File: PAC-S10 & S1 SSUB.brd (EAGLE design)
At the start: 160 x 100 mm, 177 parts, among them IC1 TLV1117, IC10 LM324D, IC14 TC51832F-10, IC15 315-5476A, IC21 TC51832F-10, IC33 LC7881M, IC34 NJM844GD, IC35 MC33079D, IC37 LM4558D, IC38 LM4558D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

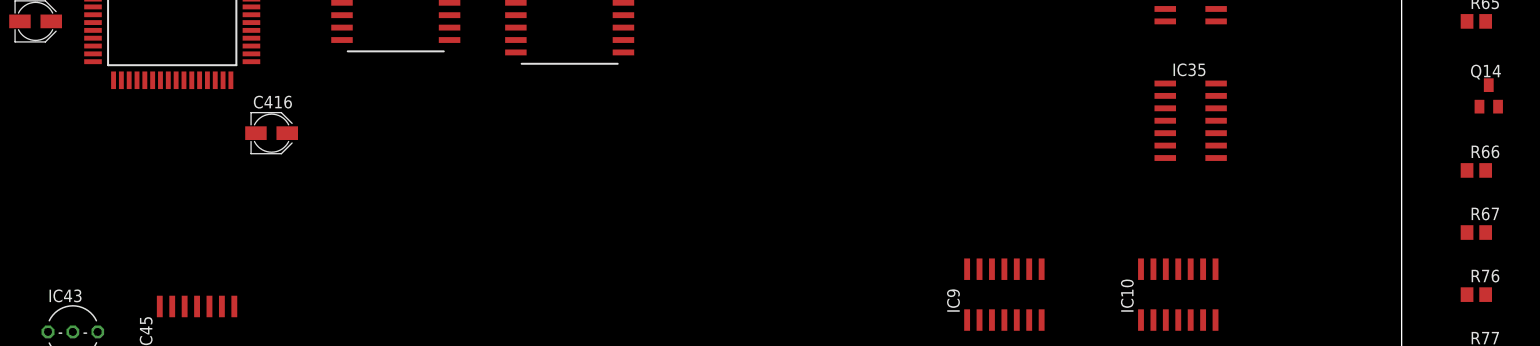
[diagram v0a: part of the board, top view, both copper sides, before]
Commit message: Add files via upload
Q14 is diode connected, uploading corrected files
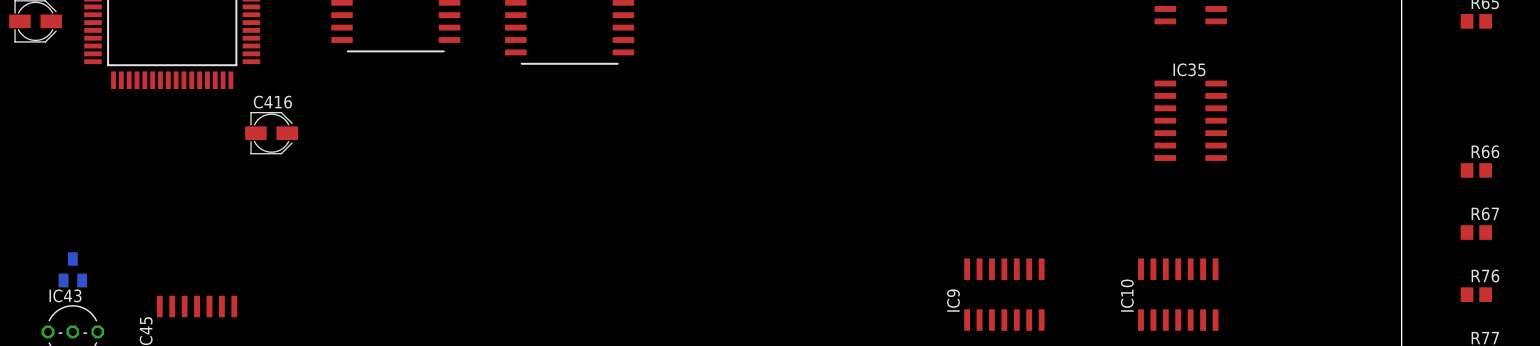
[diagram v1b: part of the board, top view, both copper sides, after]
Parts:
- moved Q14 145.9 mm to (24.1, 17.8), flipped to the bottom
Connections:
- removed net N$23: IC43.3, Q14.C, R65.2, R66.1
- net MRES: now also IC43.3, Q14.C, R65.2, R66.1
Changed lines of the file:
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@@
 <attribute name="VALUE" x="167.005" y="40.64" size="1.27" layer="27"/>
 </element>
-<element name="Q14" library="transistor-pnp" library_urn="urn:adsk.eagle:library:399" package="SOT23-BEC" package3d_urn="urn:adsk.eagle:package:28748/2" value="MMBT3906LT1SMD" x="168.91" y="35.56" smashed="yes">
-<attribute name="NAME" x="167.005" y="37.465" size="1.27" layer="25"/>
-<attribute name="POPULARITY" value="6" x="168.91" y="35.56" size="1.778" layer="27" display="off"/>
-<attribute name="VALUE" x="167.005" y="32.385" size="1.27" layer="27"/>
+<element name="Q14" library="transistor-pnp" library_urn="urn:adsk.eagle:library:399" package="SOT23-BEC" package3d_urn="urn:adsk.eagle:package:28748/2" value="MMBT3906LT1SMD" x="24.13" y="17.78" smashed="yes" rot="MR0">
+<attribute name="NAME" x="26.035" y="19.685" size="1.27" layer="26" rot="MR0"/>
+<attribute name="POPULARITY" value="6" x="24.13" y="17.78" size="1.778" layer="28" rot="MR0" display="off"/>
+<attribute name="VALUE" x="26.035" y="14.605" size="1.27" layer="28" rot="MR0"/>
 </element>
 <element name="R66" library="rcl" library_urn="urn:adsk.eagle:library:334" package="R0805" package3d_urn="urn:adsk.eagle:package:23553/2" value="10k" x="167.64" y="27.94" smashed="yes">
@@
 <contactref element="C415" pad="+"/>
 <contactref element="C416" pad="+"/>
-<contactref element="IC43" pad="1"/>
-<contactref element="R65" pad="1"/>
-<contactref element="Q14" pad="E"/>
 <contactref element="R76" pad="2"/>
 <contactref element="IC45" pad="4"/>
@@
 <contactref element="C412" pad="1"/>
 <contactref element="C423" pad="1"/>
-<wire x1="71.12" y1="-8.57" x2="64.77" y2="-8.57" width="0" layer="19" extent="1-1"/>
-<wire x1="33.02" y1="-8.57" x2="64.77" y2="-8.57" width="0" layer="19" extent="1-1"/>
-<wire x1="26.67" y1="-8.57" x2="33.02" y2="-8.57" width="0" layer="19" extent="1-1"/>
-<wire x1="20.32" y1="-8.57" x2="26.67" y2="-8.57" width="0" layer="19" extent="1-1"/>
-<wire x1="109.22" y1="-8.57" x2="71.12" y2="-8.57" width="0" layer="19" extent="1-1"/>
-<wire x1="115.57" y1="-8.57" x2="109.22" y2="-8.57" width="0" layer="19" extent="1-1"/>
-<wire x1="121.92" y1="-8.57" x2="115.57" y2="-8.57" width="0" layer="19" extent="1-1"/>
-<wire x1="-108.89" y1="-6.35" x2="121.92" y2="-8.57" width="0" layer="19" extent="1-1"/>
-<wire x1="-101.27" y1="-6.35" x2="-108.89" y2="-6.35" width="0" layer="19" extent="1-1"/>
-<wire x1="-93.65" y1="-6.35" x2="-101.27" y2="-6.35" width="0" layer="19" extent="1-1"/>
-<wire x1="-86.03" y1="-6.35" x2="-93.65" y2="-6.35" width="0" layer="19" extent="1-1"/>
-<wire x1="-78.41" y1="-6.35" x2="-86.03" y2="-6.35" width="0" layer="19" extent="1-1"/>
-<wire x1="-70.79" y1="-6.35" x2="-78.41" y2="-6.35" width="0" layer="19" extent="1-1"/>
-<wire x1="-17.45" y1="-6.35" x2="-70.79" y2="-6.35" width="0" layer="19" extent="1-1"/>
-<wire x1="-2.21" y1="-6.35" x2="-17.45" y2="-6.35" width="0" layer="19" extent="1-1"/>
-<wire x1="21.59" y1="11.43" x2="-2.21" y2="-6.35" width="0" layer="19" extent="1-1"/>
-<wire x1="36.83" y1="8.83" x2="21.59" y2="11.43" width="0" layer="19" extent="1-1"/>
+<contactref element="IC43" pad="1"/>
+<contactref element="R65" pad="1"/>
+<contactref element="Q14" pad="E"/>
+<wire x1="136.21" y1="80.01" x2="127.5334" y2="88.265" width="0" layer="19" extent="1-16"/>
+<wire x1="166.69" y1="43.18" x2="136.21" y2="80.01" width="0" layer="19" extent="1-16"/>
+<wire x1="168.59" y1="15.24" x2="166.69" y2="43.18" width="0" layer="19" extent="1-1"/>
+<wire x1="121.92" y1="-8.57" x2="168.59" y2="15.24" width="0" layer="19" extent="1-16"/>
+<wire x1="115.57" y1="-8.57" x2="121.92" y2="-8.57" width="0" layer="19" extent="16-16"/>
+<wire x1="109.22" y1="-8.57" x2="115.57" y2="-8.57" width="0" layer="19" extent="16-16"/>
+<wire x1="71.12" y1="-8.57" x2="109.22" y2="-8.57" width="0" layer="19" extent="16-16"/>
+<wire x1="64.77" y1="-8.57" x2="71.12" y2="-8.57" width="0" layer="19" extent="16-16"/>
+<wire x1="33.02" y1="-8.57" x2="64.77" y2="-8.57" width="0" layer="19" extent="16-16"/>
+<wire x1="26.67" y1="-8.57" x2="33.02" y2="-8.57" width="0" layer="19" extent="16-16"/>
+<wire x1="20.32" y1="-8.57" x2="26.67" y2="-8.57" width="0" layer="19" extent="16-16"/>
+<wire x1="36.83" y1="8.83" x2="33.02" y2="-8.57" width="0" layer="19" extent="1-16"/>
+<wire x1="21.59" y1="11.43" x2="36.83" y2="8.83" width="0" layer="19" extent="1-1"/>
+<wire x1="23.18" y1="16.68" x2="21.59" y2="11.43" width="0" layer="19" extent="16-16"/>
+<wire x1="-2.21" y1="-6.35" x2="20.32" y2="-8.57" width="0" layer="19" extent="1-16"/>
+<wire x1="-17.45" y1="-6.35" x2="-2.21" y2="-6.35" width="0" layer="19" extent="1-1"/>
 <wire x1="46.05" y1="31.75" x2="36.83" y2="8.83" width="0" layer="19" extent="1-1"/>
 <wire x1="42.39" y1="40.66" x2="46.05" y2="31.75" width="0" layer="19" extent="1-1"/>
@@
 <wire x1="40.5892" y1="88.265" x2="52.39" y2="83.82" width="0" layer="19" extent="1-16"/>
 <wire x1="25.08" y1="91.44" x2="40.5892" y2="88.265" width="0" layer="19" extent="1-16"/>
-<wire x1="127.5334" y1="88.265" x2="80.43" y2="56.515" width="0" layer="19" extent="1-1"/>
-<wire x1="136.21" y1="80.01" x2="127.5334" y2="88.265" width="0" layer="19" extent="1-16"/>
-<wire x1="166.69" y1="43.18" x2="136.21" y2="80.01" width="0" layer="19" extent="1-16"/>
-<wire x1="169.86" y1="34.46" x2="166.69" y2="43.18" width="0" layer="19" extent="1-1"/>
-<wire x1="168.59" y1="15.24" x2="169.86" y2="34.46" width="0" layer="19" extent="1-1"/>
+<wire x1="-70.79" y1="-6.35" x2="-17.45" y2="-6.35" width="0" layer="19" extent="1-1"/>
+<wire x1="-78.41" y1="-6.35" x2="-70.79" y2="-6.35" width="0" layer="19" extent="1-1"/>
+<wire x1="-86.03" y1="-6.35" x2="-78.41" y2="-6.35" width="0" layer="19" extent="1-1"/>
+<wire x1="-93.65" y1="-6.35" x2="-86.03" y2="-6.35" width="0" layer="19" extent="1-1"/>
+<wire x1="-101.27" y1="-6.35" x2="-93.65" y2="-6.35" width="0" layer="19" extent="1-1"/>
+<wire x1="-108.89" y1="-6.35" x2="-101.27" y2="-6.35" width="0" layer="19" extent="1-1"/>
 </signal>
 <signal name="N$6">
@@
 <contactref element="SUB_CN" pad="68"/>
 <contactref element="C135" pad="+"/>
-<wire x1="7.62" y1="41.91" x2="167.96" y2="34.46" width="0" layer="19" extent="1-1"/>
+<contactref element="R65" pad="2"/>
+<contactref element="IC43" pad="3"/>
+<contactref element="Q14" pad="C"/>
+<contactref element="R66" pad="1"/>
+<wire x1="24.13" y1="18.88" x2="168.59" y2="43.18" width="0" layer="19" extent="1-1"/>
+<wire x1="25.08" y1="16.68" x2="24.13" y2="18.88" width="0" layer="19" extent="1-1"/>
+<wire x1="166.69" y1="27.94" x2="25.08" y2="16.68" width="0" layer="19" extent="1-1"/>
+<wire x1="26.67" y1="11.43" x2="166.69" y2="27.94" width="0" layer="19" extent="1-1"/>
+<wire x1="7.62" y1="41.91" x2="26.67" y2="11.43" width="0" layer="19" extent="1-1"/>
 <wire x1="-124.13" y1="-6.35" x2="7.62" y2="41.91" width="0" layer="19" extent="1-1"/>
 </signal>
@@
 <wire x1="33.02" y1="14.03" x2="168.59" y2="21.59" width="0" layer="19" extent="1-1"/>
 </signal>
-<signal name="N$23">
-<contactref element="R65" pad="2"/>
-<contactref element="IC43" pad="3"/>
-<contactref element="Q14" pad="C"/>
-<contactref element="R66" pad="1"/>
-<wire x1="168.91" y1="36.66" x2="166.69" y2="27.94" width="0" layer="19" extent="1-1"/>
-<wire x1="168.59" y1="43.18" x2="168.91" y2="36.66" width="0" layer="19" extent="1-1"/>
-<wire x1="26.67" y1="11.43" x2="168.59" y2="43.18" width="0" layer="19" extent="1-1"/>
-</signal>
 <signal name="N$12">

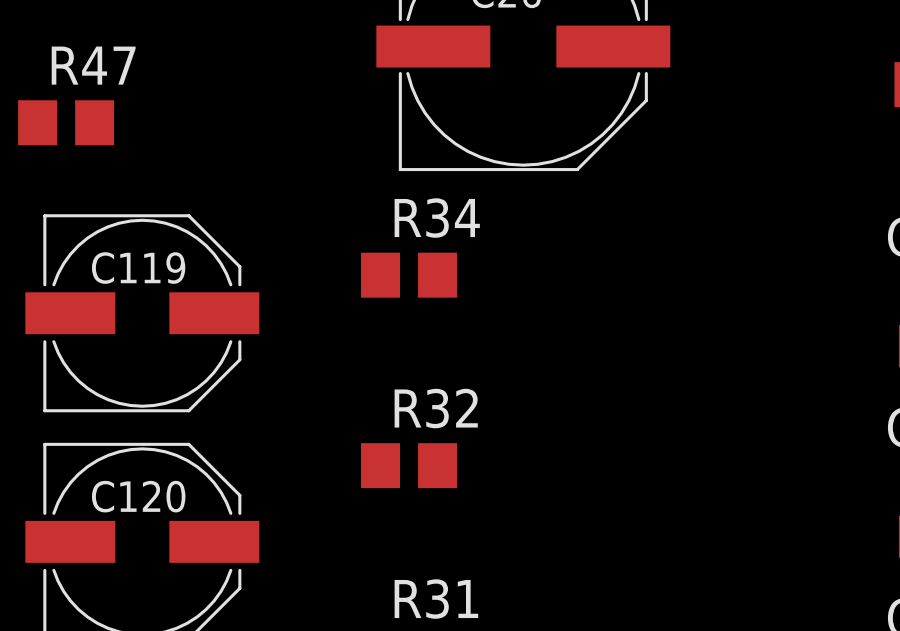
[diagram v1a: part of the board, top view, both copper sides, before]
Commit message: Add files via upload
Corrected resistor reference designators (R32, R34)
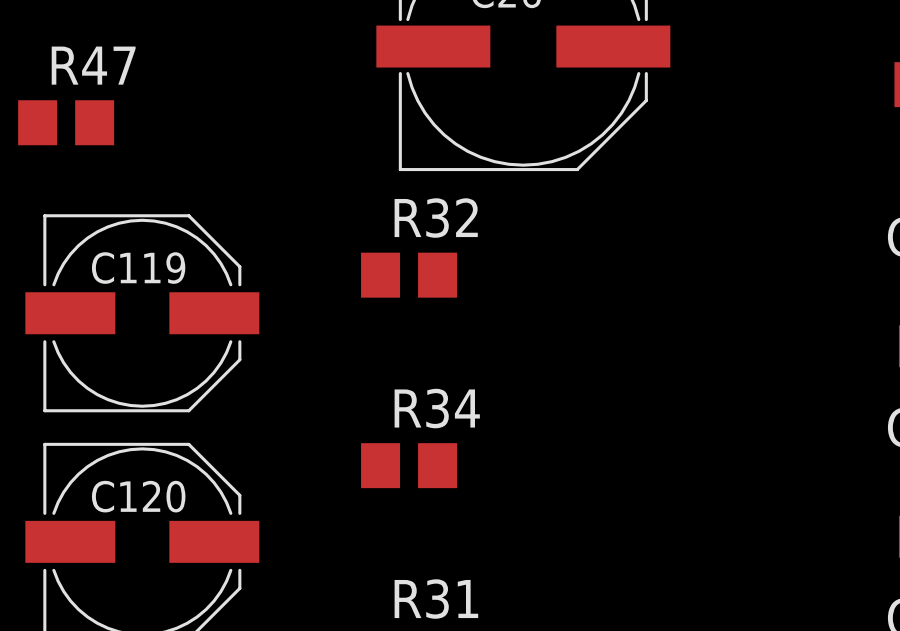
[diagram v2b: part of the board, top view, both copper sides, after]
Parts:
- R32: value 100k -> 33k
- R34: value 33k -> 100k
- moved R32 6.35 mm to (125.7, 142.2)
- moved R34 6.35 mm to (125.7, 135.9)
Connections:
- net CART_R+: now also R34.2; no longer R32.2
- net N$46: now also R32.2, R34.1; no longer R32.1, R34.2
- net N$49: now also R32.1; no longer R34.1
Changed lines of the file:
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@@
 <attribute name="VALUE" x="127.74" y="147.635" size="1.016" layer="27"/>
 </element>
-<element name="R34" library="rcl" library_urn="urn:adsk.eagle:library:334" package="R0805" package3d_urn="urn:adsk.eagle:package:23553/2" value="33k" x="125.73" y="142.24" smashed="yes">
+<element name="R32" library="rcl" library_urn="urn:adsk.eagle:library:334" package="R0805" package3d_urn="urn:adsk.eagle:package:23553/2" value="33k" x="125.73" y="142.24" smashed="yes">
 <attribute name="NAME" x="125.095" y="143.51" size="1.27" layer="25"/>
 <attribute name="POPULARITY" value="85" x="125.73" y="142.24" size="1.778" layer="27" display="off"/>
@@
 <attribute name="VALUE" x="125.095" y="139.7" size="1.27" layer="27"/>
 </element>
-<element name="R32" library="rcl" library_urn="urn:adsk.eagle:library:334" package="R0805" package3d_urn="urn:adsk.eagle:package:23553/2" value="100k" x="125.73" y="135.89" smashed="yes">
+<element name="R34" library="rcl" library_urn="urn:adsk.eagle:library:334" package="R0805" package3d_urn="urn:adsk.eagle:package:23553/2" value="100k" x="125.73" y="135.89" smashed="yes">
 <attribute name="NAME" x="125.095" y="137.16" size="1.27" layer="25"/>
 <attribute name="POPULARITY" value="85" x="125.73" y="135.89" size="1.778" layer="27" display="off"/>
@@
 <contactref element="C20" pad="2"/>
 <contactref element="R30" pad="2"/>
-<contactref element="R34" pad="1"/>
+<contactref element="R32" pad="1"/>
 <wire x1="50.48" y1="113.03" x2="124.78" y2="142.24" width="0" layer="19" extent="1-1"/>
 <wire x1="50.48" y1="119.38" x2="50.48" y2="113.03" width="0" layer="19" extent="1-1"/>
@@
 <signal name="N$46">
 <contactref element="IC10" pad="9"/>
-<contactref element="R34" pad="2"/>
-<contactref element="R32" pad="1"/>
+<contactref element="R32" pad="2"/>
+<contactref element="R34" pad="1"/>
 <wire x1="126.68" y1="142.24" x2="124.78" y2="135.89" width="0" layer="19" extent="1-1"/>
 <wire x1="139.7" y1="17.84" x2="126.68" y2="142.24" width="0" layer="19" extent="1-1"/>
 </signal>
 <signal name="CART_R+">
-<contactref element="R32" pad="2"/>
+<contactref element="R34" pad="2"/>
 <contactref element="IC10" pad="8"/>
 <contactref element="C118" pad="+"/>
